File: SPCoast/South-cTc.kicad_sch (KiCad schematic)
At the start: 6 parts

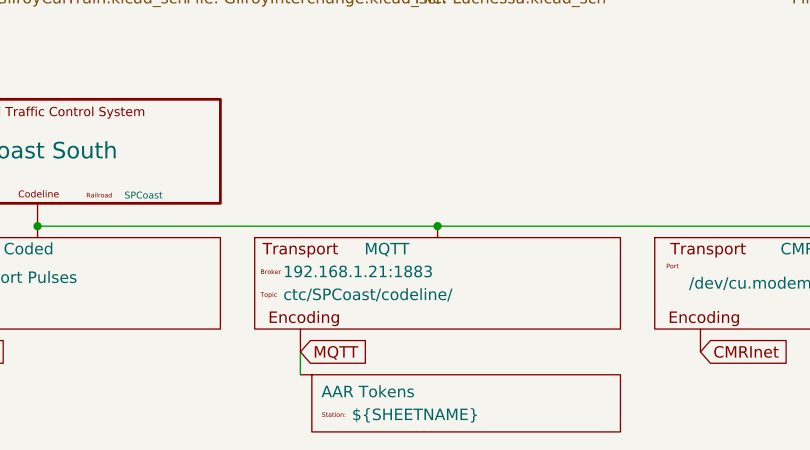
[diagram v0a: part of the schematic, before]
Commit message: chore(kicad): SPCoast symbols refreshed, field attribute visibility, no-connects on unused pins (owner's edit, baseline)
Owner, 2026-10-08: updated symbols from the libraries (the field pin direction flip, InterlockingPlant
61269e0), adjusted attribute visibility, added 22 no-connect markers on unused pins.

Verified (committed as saved, no edits):
- 485 components, 648 nets; every net identical to the previous commit.
- ERC 53 -> 20 messages (13 errors, 7 warnings). Remaining: unconnected HOUSE H / aux MC pins
  (Gilroy Caltrain, Luchessa, Watsonville); Corporal SW11901 still Railroad:Switch_HandThrow (not in
  the library) with open N/R legs; Sargent switch 1 open N/R legs; Christopher Panel U10029 A6 open
  while lamp LMP10093 carries a no-connect; 5 inherited wire stubs.
- Every instance path starts at the root uuid.

Co-Authored-By: Claude Opus 5.5 <noreply@anthropic.com>
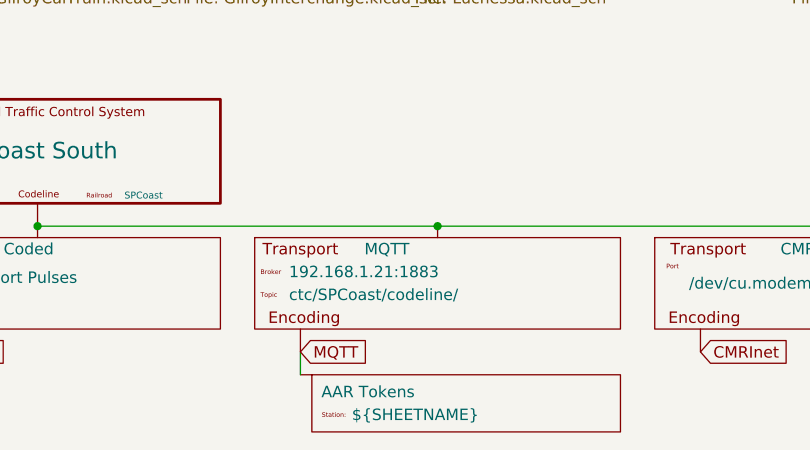
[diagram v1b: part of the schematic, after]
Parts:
- Transport2006: Station (none) -> ${SHEETNAME}
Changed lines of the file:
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@@
 		)
 		(property "Broker" "192.168.1.21:1883"
-			(at 66.675 153.67 0)
+			(at 67.31 153.67 0)
 			(show_name no)
 			(do_not_autoplace yes)
@@
 		)
 		(property "Topic" "ctc/${Railroad}/codeline/"
-			(at 66.675 156.21 0)
+			(at 67.31 156.21 0)
 			(show_name no)
 			(do_not_autoplace yes)
@@
 		(property "Railroad" "SPCoast"
 			(at 55.88 154.305 0)
+			(hide yes)
+			(show_name no)
+			(do_not_autoplace no)
+			(effects
+				(font
+					(size 1.27 1.27)
+				)
+			)
+		)
+		(property "Station" "${SHEETNAME}"
+			(at 58.42 156.845 0)
 			(hide yes)
 			(show_name no)
@@
 			(at 154.94 154.94 0)
 			(show_name no)
-			(do_not_autoplace no)
-			(effects
-				(font
+			(do_not_autoplace yes)
+			(effects
+				(font

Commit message: feat(spcoast): every sheet on the four Railroad libraries (checkpoint step 6, mechanical half)
By SPCoast/edits/2026-10-12-migrate-libraries.py, run once with KiCad closed: 483 instances
remapped across 16 sheets, embedded definitions replaced by the library blocks, instance fields
synced (Kind, ControlToken, Vital, NormalIs, Chain, Index dropped; Indications renamed
IndicationCeiling; Hold_ms renamed hold_ms; a pixel's Index became its Address; Rulebook kept
on the four Luchessa markers because the compiler still reads it), and 22 units added at the
same position for the plates and devices that are multi-unit now. Owner's choices: every plant
head CPL; Sargent's semaphore UQ; the 0x27 PCA9685 as PWM; the office MAX7313s as the
SPCoastcTc variant. Left by hand: the two AUXILIARY_TRAFFIC markers on Watsonville (retired).

Verified (production/migration-gate.txt, netlist_diff.py against pre-migration.net): office
and local plates and all chips keep their connectivity; 14 nets lost, all on Sargent, where
the six field devices (DevSW13001, 13004 to 13007, 13012) have new pin positions and must be
re-wired by hand. ERC: lib_symbol_issues 492 before (unregistered libraries) to 2 after (the
retired markers); the 29 unconnected pins are those devices and their chip pins.

Co-Authored-By: Claude Fable 5.1 <noreply@anthropic.com>
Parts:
- Encoding2001: symbol RailroadPanel:Codeline-Encoding-AAR -> Railroad-Office:Codeline-Encoding-AAR
- MACHINE2002: symbol RailroadPanel:CtcMachine -> Railroad-Office:CtcMachine
- Transport2005: symbol RailroadPanel:Codeline-Transport-TimeCode -> Railroad-Office:Codeline-Transport-TimeCode
- Transport2006: symbol RailroadPanel:Codeline-Transport-MQTT -> Railroad-Office:Codeline-Transport-MQTT
- Transport2007: symbol RailroadPanel:Codeline-Transport-CMRInet -> Railroad-Office:Codeline-Transport-CMRInet
- Transport2008: symbol RailroadPanel:Codeline-Transport-Loconet -> Railroad-Office:Codeline-Transport-Loconet
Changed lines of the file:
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@@
 	)
 	(symbol
-		(lib_id "RailroadPanel:Codeline-Transport-MQTT")
+		(lib_id "Railroad-Office:Codeline-Transport-MQTT")
 		(at 83.82 148.59 0)
 		(unit 1)
@@
 	)
 	(symbol
-		(lib_id "RailroadPanel:CtcMachine")
+		(lib_id "Railroad-Office:CtcMachine")
 		(at 39.37 140.97 0)
 		(unit 1)
@@
 	)
 	(symbol
-		(lib_id "RailroadPanel:Codeline-Transport-TimeCode")
+		(lib_id "Railroad-Office:Codeline-Transport-TimeCode")
 		(at 39.37 148.59 0)
 		(unit 1)
@@
 	)
 	(symbol
-		(lib_id "RailroadPanel:Codeline-Encoding-AAR")
+		(lib_id "Railroad-Office:Codeline-Encoding-AAR")
 		(at 68.58 165.1 0)
 		(unit 1)
@@
 	)
 	(symbol
-		(lib_id "RailroadPanel:Codeline-Transport-CMRInet")
+		(lib_id "Railroad-Office:Codeline-Transport-CMRInet")
 		(at 128.27 151.13 0)
 		(unit 1)
@@
 	)
 	(symbol
-		(lib_id "RailroadPanel:Codeline-Transport-Loconet")
+		(lib_id "Railroad-Office:Codeline-Transport-Loconet")
 		(at 171.45 148.59 0)
 		(unit 1)

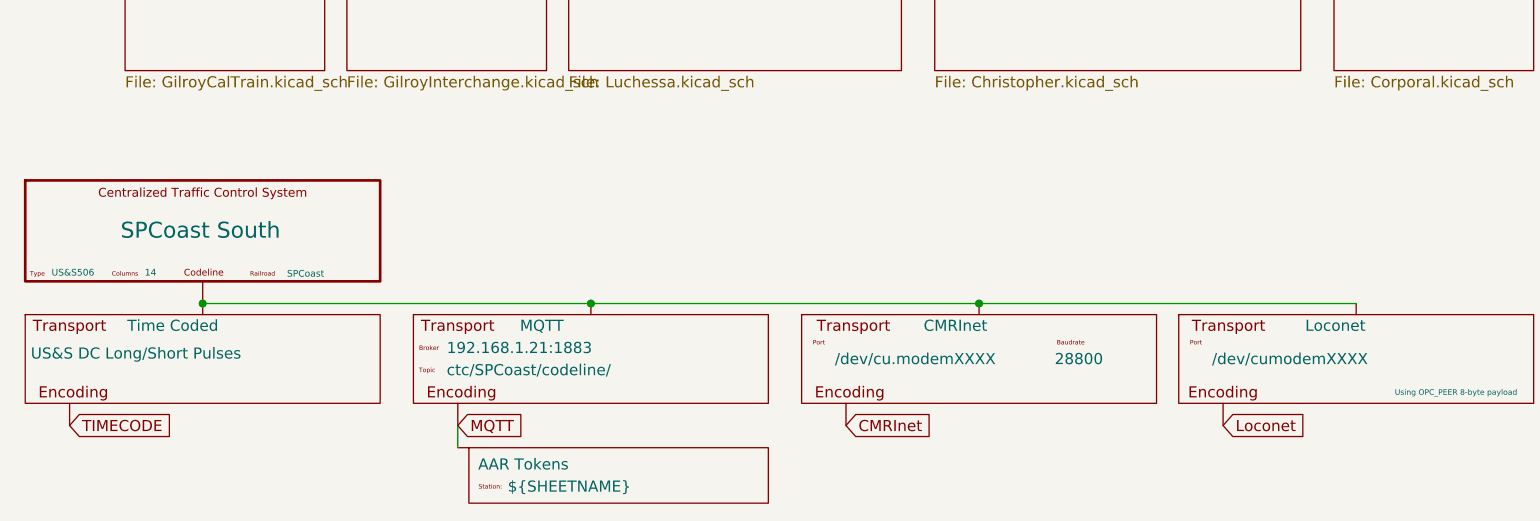
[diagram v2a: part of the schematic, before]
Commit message: chore: owner's Sargent cleanup and library edits of 2026-10-12 and 13 (baseline)
Co-Authored-By: Claude Fable 5.1 <noreply@anthropic.com>
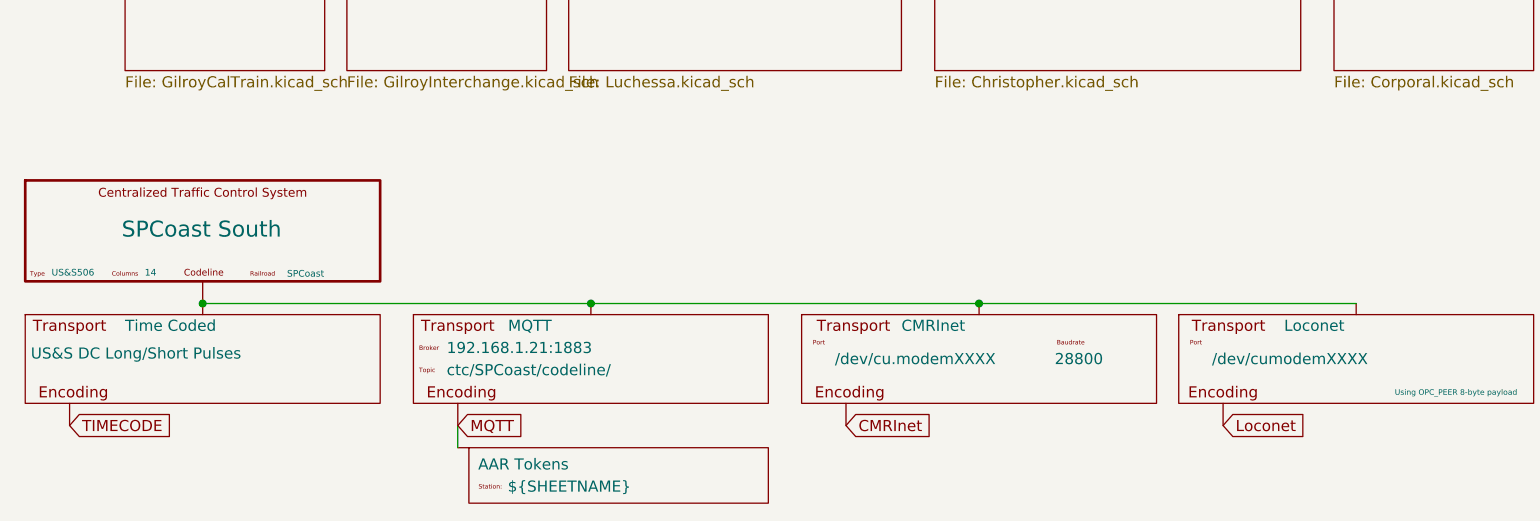
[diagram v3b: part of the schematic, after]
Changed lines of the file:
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@@
 		)
 		(property "Value" "MQTT"
-			(at 75.692 151.13 0)
-			(show_name no)
-			(do_not_autoplace no)
-			(effects
-				(font
-					(size 1.27 1.27)
-				)
-				(justify left)
+			(at 76.835 151.13 0)
+			(show_name no)
+			(do_not_autoplace no)
+			(effects
+				(font
+					(size 1.27 1.27)
+				)
 			)
 		)
@@
 			(hide yes)
 			(show_name no)
-			(do_not_autoplace no)
+			(do_not_autoplace yes)
 			(effects
 				(font
@@
 		)
 		(property "Value" "SPCoast South"
-			(at 39.116 140.208 0)
+			(at 39.243 140.081 0)
 			(show_name no)
 			(do_not_autoplace yes)
@@
 		)
 		(property "Value" "Time Coded"
-			(at 30.734 151.13 0)
+			(at 30.48 151.13 0)
 			(show_name no)
 			(do_not_autoplace yes)
@@
 		)
 		(property "Value" "CMRInet"
-			(at 121.92 151.13 0)
+			(at 119.38 151.13 0)
 			(show_name no)
 			(do_not_autoplace yes)
@@
 		)
 		(property "Value" "Loconet"
-			(at 165.608 151.13 0)
-			(show_name no)
-			(do_not_autoplace yes)
+			(at 163.195 151.13 0)
+			(show_name no)
+			(do_not_autoplace yes)

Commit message: feat(kicad): Processor declares the Caltrain CMRInet node; drivers carry Bit only (ADR 0005)
ADR 0005 §9 applied by SPCoast/edits/2026-10-19-processor-node.py:
- Railroad-HardwareIO: new Processor symbol (Role STRUCTURE, Kind
  PROCESSOR, no pins; Board, Transport, Address); Driver-CMRI-IB/OB lose
  UA and Address, Value renders IN.${Bit} / OUT.${Bit}, body text and
  Description follow.
- Railroad-Office: every Codeline-Transport-* gains Host (empty = the
  office processor).
- Gilroy Caltrain: one Processor "Caltrain" (Transport CMRInet, Address
  30, Board cpNode) placed right of the Interlocking box; the 34 CMRI
  drivers lose UA and Address (68 field values); embedded definitions of
  the three symbols refreshed.
- South-cTc: the MQTT transport loses Station (an encoding fact, ADR
  0001); the four transports gain Host ""; their embedded definitions
  refreshed.

Verified: gate script 2026-10-19-processor-node-gate.py PASS on
production/pre-processor.net vs post-processor.net exported from
SPCoast.kicad_sch (716 nets unchanged, 586 -> 587 parts, exactly the
expected field delta, no other field change, ERC zero before and after);
its --self-test shows the gate fails on a leftover UA, a dropped net and
an unrelated field change. KiCad's forced resave on copies is
byte-identical for both libraries and South-cTc; GilroyCalTrain was
adopted from that resave after checking only the new block's position
differed. Subdivision Role lint: 91 symbols, 0 errors; kicad-cli sym
export svg of Processor and the sheet checked by eye. No lock files;
KiCad closed by the owner.

Co-Authored-By: Claude Fable 5.1 <noreply@anthropic.com>
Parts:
- Transport2006: Station ${SHEETNAME} -> (none)
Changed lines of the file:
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@@
 			)
 		)
-		(property "Station" "${SHEETNAME}"
-			(at 58.42 156.845 0)
-			(hide yes)
-			(show_name no)
-			(do_not_autoplace yes)
+		(property "Host" ""
+			(at 83.82 148.59 0)
+			(hide yes)
+			(show_name no)
+			(do_not_autoplace no)
 			(effects
 				(font
@@
 			)
 		)
+		(property "Host" ""
+			(at 39.37 148.59 0)
+			(hide yes)
+			(show_name no)
+			(do_not_autoplace no)
+			(effects
+				(font
+					(size 1.27 1.27)
+				)
+			)
+		)
 		(pin "2"
 		)
@@
 			)
 		)
+		(property "Host" ""
+			(at 128.27 151.13 0)
+			(hide yes)
+			(show_name no)
+			(do_not_autoplace no)
+			(effects
+				(font
+					(size 1.27 1.27)
+				)
+			)
+		)
 		(pin "2"
 		)
@@
 			)
 		)
+		(property "Host" ""
+			(at 171.45 148.59 0)
+			(hide yes)
+			(show_name no)
+			(do_not_autoplace no)
+			(effects
+				(font
+					(size 1.27 1.27)
+				)
+			)
+		)
